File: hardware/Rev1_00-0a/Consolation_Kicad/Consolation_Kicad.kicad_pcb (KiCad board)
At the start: 6 copper layers, 137.5 x 76.6 mm, 401 parts, among them J10 61300311121, J11 5051102291, J12 RPI_CMx_B, J13 5051102291, J14 61300311121, J15 61300311121, J17 61300311121, J18 61300411121, J19 RPI_CMx_A, J2 SJ-3524-SMT-TR, J3 62684-402100ALF, J4 12401598E4#2A, J5 S2B-PH-K-S, J6 2086581001, J7 2998TR, J8 DM3AT-SF-PEJM5, Q1 SSM3K56FS,LF, Q10 SSM3K56FS,LF, Q11 SSM3K56FS,LF, Q14 SSM3K56FS,LF, Q18 SSM3K56FS,LF, Q19 SSM3K56FS,LF, Q2 SSM3K56FS,LF, Q20 SSM3K56FS,LF, Q21 SSM3K56FS,LF, Q22 SSM3K56FS,LF, Q23 SSM3K56FS,LF, Q24 SSM3K56FS,LF, Q25 SSM3K56FS,LF, Q26 SSM3K56FS,LF, Q27 SSM3K56FS,LF, Q28 SSM3K56FS,LF, Q3 SSM3K56FS,LF, Q7 SSM3K56FS,LF, Q8 SSM3K56FS,LF, Q9 SSM3K56FS,LF, U1 BQ25640VDLR, U10 TPS62826DMQR, U11 AP22913W6-7, U15 SN65DSI84ZXHR, U18 AP22913W6-7, U19 SN74LVC1G125DBVR, U2 RP2350A, U21 MCP7940NT-I/MS, U26 TPS61169DCKR, U30 STM6710DWB6F, U31 SN74LVC1G125DBVR, U32 SN74HCS365QPWRQ1, U4 ECS-2016MVQ-120-BP-TR, U5 NAU88C22YG, U6 AP22913W6-7, U7 TPS79901DRVR, U8 GD25Q32CWIGR, U9 TPS61230ARNSR, Y1 12MHz 10pF, Y2 32.768kHz

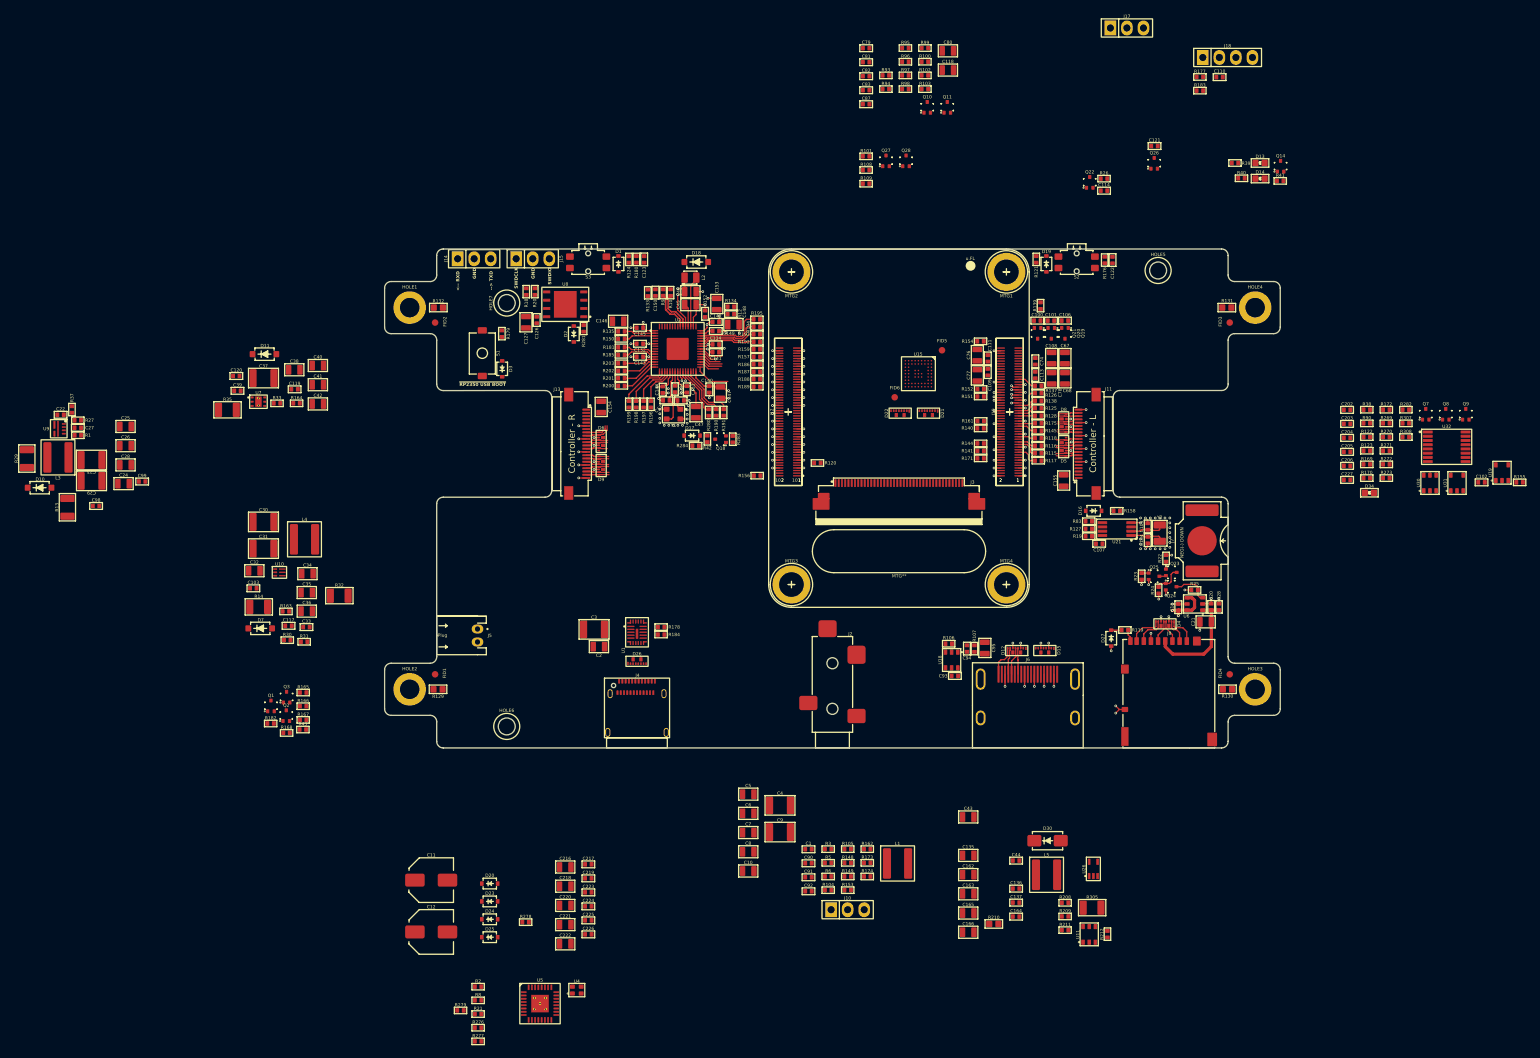
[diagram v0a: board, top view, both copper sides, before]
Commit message: Continue preliminary placement To do : Power supplies + Type C charger
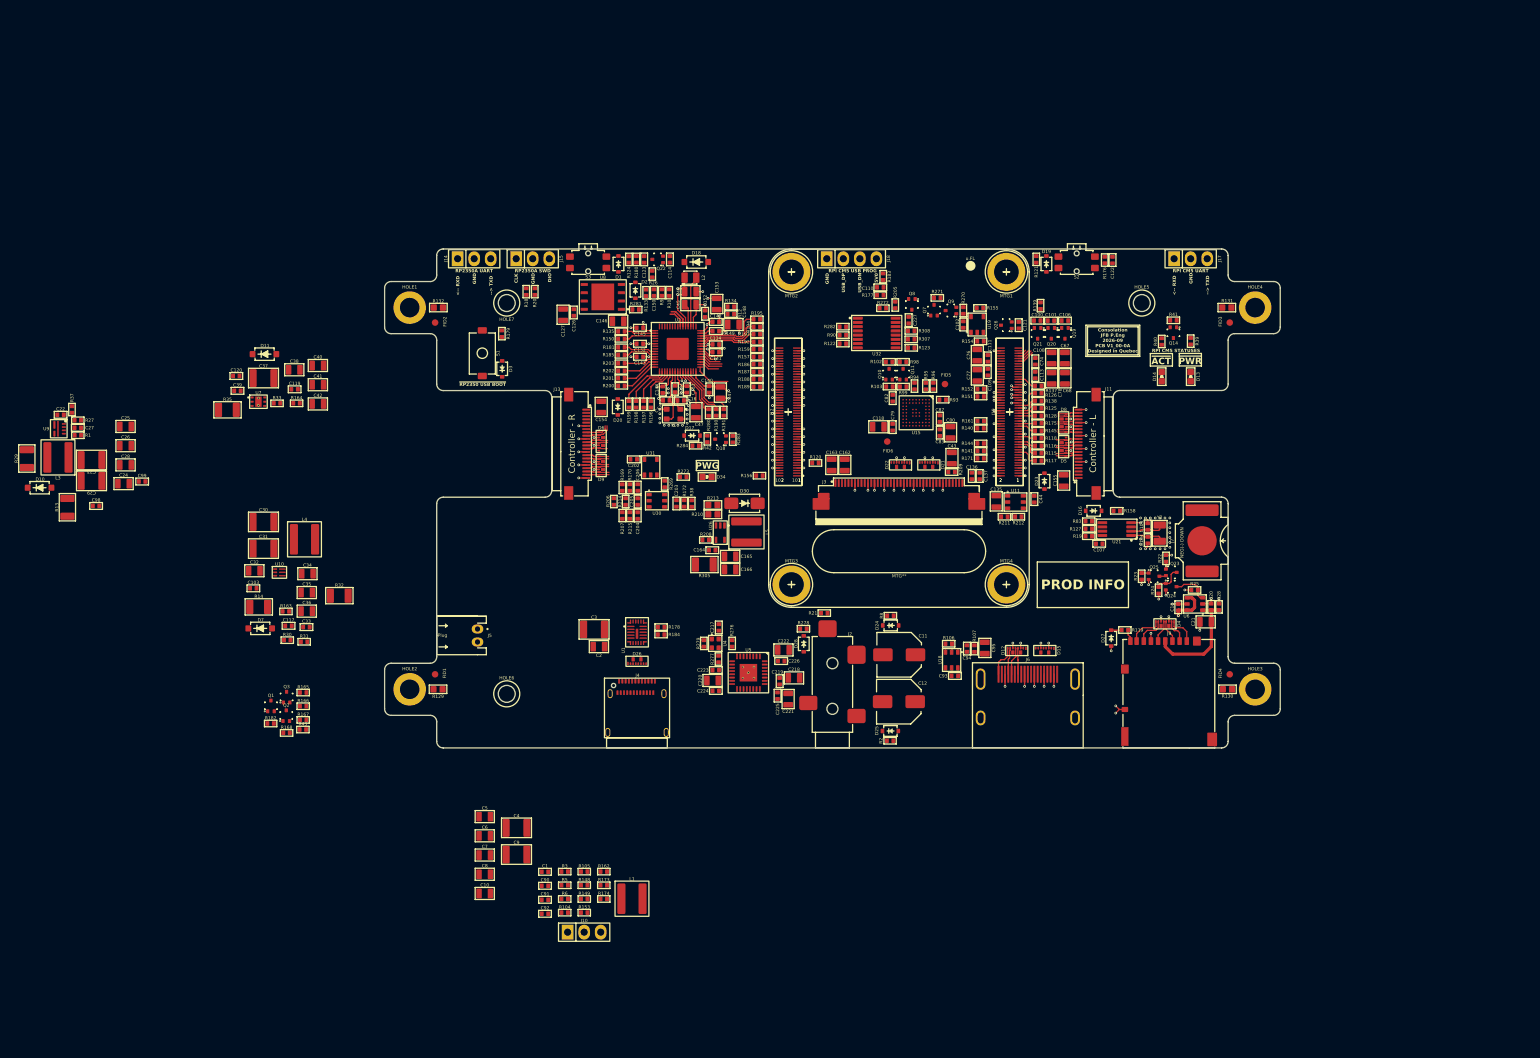
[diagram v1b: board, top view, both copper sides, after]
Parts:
- removed C216: 10u, footprint:CAP_NONPOL_0805
- removed C81: 0.1u, footprint:CAP_NONPOL_0402
- removed Q27, Q28: SSM3K56FS,LF, footprint:SC-75
- removed R100, R101, R108: 10K, footprint:RES_0402
- removed R109, R97: 0R, footprint:RES_0402
- added D28: ESD7351HT1G, footprint:SOD-323, F.Cu at (104.5, 110.7)
- added R205: 6K04, footprint:RES_0402, F.Cu at (118.5, 58.7)
- added R206: 0R, footprint:RES_0402, F.Cu at (75.3, 88.9)
- added R207: 0R, footprint:RES_0402, F.Cu at (76.6, 91.0)
- added R213: 1R5, footprint:RES_0603, F.Cu at (90.5, 89.4)
- added R214: 0R, footprint:RES_0402, F.Cu at (77.1, 88.9)
- added R215: 0R, footprint:RES_0402, F.Cu at (77.8, 91.0)
- R95, R96: value 0R -> 10K
- moved U31 123.8 mm to (81.0, 83.6)
- moved U30 118.7 mm to (81.9, 88.8), turned to -90 degrees
- moved R169 114.3 mm to (76.6, 86.7), turned to 90 degrees
- moved R170 113.1 mm to (77.8, 86.7), turned to -90 degrees
- moved R269 111.2 mm to (83.1, 86.2), turned to 90 degrees
- moved C202 109.8 mm to (78.3, 82.4)
- moved C204 109.6 mm to (79.0, 91.0), turned to 90 degrees
- moved C205 109.2 mm to (79.0, 88.9), turned to 90 degrees
- moved C206 109.0 mm to (79.0, 86.7), turned to -90 degrees
- moved R172 108.7 mm to (86.1, 89.2), turned to -90 degrees
- moved R273 107.9 mm to (86.0, 85.1)
- moved D23 106.8 mm to (141.4, 85.8), turned to -90 degrees
- moved R38 104.6 mm to (87.2, 89.2), turned to 90 degrees
- moved C203 103.7 mm to (84.9, 89.2), turned to -90 degrees
- moved D34 101.7 mm to (89.6, 85.1), turned to 180 degrees
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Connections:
- C204 pad 2: 1V8 -> Net-(U30-V3IN)
- C205 pad 2: 3V3 -> Net-(U30-V2IN)
- R272 pad 1: Net-(Q8-D) -> GND
- R272 pad 2: 3V3 -> Net-(Q8-D)
- R95 pad 1: 1V8 -> /DSI TO LVDS/SN65DSI_EN
- R95 pad 2: Net-(U15-ADDR) -> /~{DSI_BRDG_RST}
- R96 pad 1: unconnected-(R96-Pad1) -> GND
- R96 pad 2: Net-(U15-IRQ) -> /DSI TO LVDS/SN65DSI_EN
- U15 pad J9: Net-(U15-IRQ) -> unconnected-(U15-IRQ-PadJ9)
- U30 pad 2: 3V3 -> Net-(U30-V2IN)
- U30 pad 3: 1V8 -> Net-(U30-V3IN)
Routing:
- net GND: track 120.3 -> 134.4 mm, vias 139 -> 153
- net /CONTROLLER/USB_P: track 6.20 -> 2.93 mm
- net /CONTROLLER/USB_N: track 6.20 -> 3.40 mm
- net /CM5_CONN_A/~{WL_DIS}: track 0.00 -> 2.71 mm
- net /CM5_CONN_A/~{BT_DIS}: track 0.00 -> 2.45 mm
- net /CM5_CONN_A/~{RPIBOOT}: track 0.00 -> 1.98 mm
- net /CM5_CONN_A/~{RPI_LED_PWR}: track 0.00 -> 1.31 mm
- net 3V3: track 38.9 -> 38.0 mm, vias 17 -> 16
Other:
- board text added: "5V0"
- board text added: "CLK"
- board text added: "Consolation JFB P.Eng 2026-09 PCB V1_00-0A Designed in Quebec"
- board text added: "DIO"
- board text added: "PROD INFO"
- board text added: "PWG"
- board text added: "RP2350A SWD"
- board text added: "RP2350A UART"
- board text added: "RPI CM5 STATUSES"
- board text added: "RPI CM5 UART"
- board text added: "RPI CM5 USB PROG"
- board text added: "USB_DN"
- board text added: "USB_DP"
- board text added: "~{ACT}"
- board text added: "~{PWR}"
- board text removed: "SWDCLK"
- board text removed: "SWDIO"

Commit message: Preliminary placement done Add test points to PCB
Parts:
- removed C103, C117, C120, C91, C98, C99: 0.1u, footprint:CAP_NONPOL_0402
- removed C24, C32, C38: 1u, footprint:CAP_NONPOL_0805
- removed C25, C34, C41: 22u, footprint:CAP_NONPOL_0805
- removed Q2: SSM3K56FS,LF, footprint:SC-75
- removed R165, R167: 10K, footprint:RES_0402
- removed R178, R184: 0R, footprint:RES_0402
- removed R29, R32, R35: 0R, footprint:RES_1206
- added C13: 22u, footprint:CAP_NONPOL_0805, F.Cu at (83.5, 97.5)
- added D29: SMAJ20A, footprint:DO-214AC, F.Cu at (84.8, 114.3)
- added R108: 4K7, footprint:RES_0402, F.Cu at (127.0, 65.0)
- added R7: 103AT-4-70374, footprint:HEADER_2P_2_54MM, F.Cu at (56.9, 125.2)
- added TP1: 75 mils, footprint:SMT_TP_75_MILS, B.Cu at (167.4, 66.2)
- added TP10: 75 mils, footprint:SMT_TP_75_MILS, B.Cu at (70.2, 101.6)
- added TP11: 75 mils, footprint:SMT_TP_75_MILS, B.Cu at (61.5, 90.0)
- added TP12: 75 mils, footprint:SMT_TP_75_MILS, B.Cu at (50.0, 97.8)
- added TP13: 75 mils, footprint:SMT_TP_75_MILS, B.Cu at (61.5, 94.4)
- added TP14: 75 mils, footprint:SMT_TP_75_MILS, B.Cu at (59.1, 91.5)
- added TP15: 75 mils, footprint:SMT_TP_75_MILS, B.Cu at (81.0, 79.8)
- added TP16: 75 mils, footprint:SMT_TP_75_MILS, B.Cu at (110.1, 59.3)
- added TP17: 75 mils, footprint:SMT_TP_75_MILS, B.Cu at (131.0, 56.8)
- added TP18: 75 mils, footprint:SMT_TP_75_MILS, B.Cu at (156.4, 98.0)
- added TP19: 75 mils, footprint:SMT_TP_75_MILS, B.Cu at (167.8, 107.5)
- added TP2: 75 mils, footprint:SMT_TP_75_MILS, B.Cu at (142.8, 90.8)
- added TP20: 75 mils, footprint:SMT_TP_75_MILS, B.Cu at (101.9, 108.4)
- added TP21: 75 mils, footprint:SMT_TP_75_MILS, B.Cu at (94.5, 121.0)
- added TP22: 75 mils, footprint:SMT_TP_75_MILS, B.Cu at (91.4, 121.0)
- added TP23: 75 mils, footprint:SMT_TP_75_MILS, B.Cu at (106.8, 80.3)
- added TP24: 75 mils, footprint:SMT_TP_75_MILS, B.Cu at (141.3, 56.2)
- added TP25: 75 mils, footprint:SMT_TP_75_MILS, B.Cu at (92.5, 52.8)
- added TP26: 75 mils, footprint:SMT_TP_75_MILS, B.Cu at (98.3, 110.1)
- added TP27: 75 mils, footprint:SMT_TP_75_MILS, B.Cu at (94.0, 105.8)
- added TP28: 75 mils, footprint:SMT_TP_75_MILS, B.Cu at (94.0, 102.2)
- added TP29: 75 mils, footprint:SMT_TP_75_MILS, B.Cu at (97.4, 102.0)
- added TP3: 75 mils, footprint:SMT_TP_75_MILS, B.Cu at (65.0, 114.2)
- added TP30: 75 mils, footprint:SMT_TP_75_MILS, B.Cu at (112.5, 116.0)
- added TP31: 75 mils, footprint:SMT_TP_75_MILS, B.Cu at (105.2, 123.0)
- added TP32: 75 mils, footprint:SMT_TP_75_MILS, B.Cu at (149.1, 83.8)
- added TP33: 75 mils, footprint:SMT_TP_75_MILS, B.Cu at (68.3, 76.8)
- added TP34: 75 mils, footprint:SMT_TP_75_MILS, B.Cu at (85.4, 82.5)
- added TP35: 75 mils, footprint:SMT_TP_75_MILS, B.Cu at (73.8, 61.0)
- added TP36: 75 mils, footprint:SMT_TP_75_MILS, B.Cu at (88.0, 52.4)
- added TP37: 75 mils, footprint:SMT_TP_75_MILS, B.Cu at (89.7, 112.0)
- added TP38: 75 mils, footprint:SMT_TP_75_MILS, B.Cu at (60.1, 112.7)
- added TP39: 75 mils, footprint:SMT_TP_75_MILS, B.Cu at (75.5, 114.4)
- added TP4: 75 mils, footprint:SMT_TP_75_MILS, B.Cu at (147.7, 110.5)
- added TP40: 75 mils, footprint:SMT_TP_75_MILS, B.Cu at (82.0, 114.3)
- added TP41: 75 mils, footprint:SMT_TP_75_MILS, B.Cu at (74.5, 102.3)
- added TP42: 75 mils, footprint:SMT_TP_75_MILS, B.Cu at (84.8, 101.0)
- added TP43: 75 mils, footprint:SMT_TP_75_MILS, B.Cu at (72.4, 114.7)
- added TP44: 75 mils, footprint:SMT_TP_75_MILS, B.Cu at (79.7, 101.7)
- added TP45: 75 mils, footprint:SMT_TP_75_MILS, B.Cu at (131.0, 88.4)
- added TP46: 75 mils, footprint:SMT_TP_75_MILS, B.Cu at (101.2, 89.2)
- added TP47: 75 mils, footprint:SMT_TP_75_MILS, B.Cu at (89.8, 86.3)
- added TP48: 75 mils, footprint:SMT_TP_75_MILS, B.Cu at (134.3, 115.6)
- added TP49: 75 mils, footprint:SMT_TP_75_MILS, B.Cu at (61.4, 122.7)
- added TP5: 75 mils, footprint:SMT_TP_75_MILS, B.Cu at (83.3, 93.3)
- added TP50: 75 mils, footprint:SMT_TP_75_MILS, B.Cu at (124.9, 62.9)
- added TP51: 75 mils, footprint:SMT_TP_75_MILS, B.Cu at (125.2, 68.7)
- added TP6: 75 mils, footprint:SMT_TP_75_MILS, B.Cu at (97.5, 106.5)
- added TP7: 75 mils, footprint:SMT_TP_75_MILS, B.Cu at (69.3, 68.2)
- added TP8: 75 mils, footprint:SMT_TP_75_MILS, B.Cu at (50.5, 90.8)
- added TP9: 75 mils, footprint:SMT_TP_75_MILS, B.Cu at (76.7, 99.6)
- moved Q1 117.9 mm to (127.8, 67.0), turned to 90 degrees
- moved R166 113.3 mm to (128.7, 69.2), turned to 90 degrees
- moved R37 87.1 mm to (76.8, 94.9), turned to 180 degrees
- moved R13 86.6 mm to (77.7, 97.0), turned to 180 degrees
- moved L3 83.9 mm to (72.5, 97.0), turned to 90 degrees
- moved C22 81.7 mm to (70.7, 90.7)
- moved U9 81.7 mm to (70.2, 92.8)
- moved R1 81.5 mm to (73.2, 93.0)
- moved C27 81.5 mm to (73.2, 91.8)
- moved R27 81.5 mm to (73.2, 90.7)
- moved D10 76.9 mm to (63.9, 91.9), turned to -90 degrees
- moved C29 73.7 mm to (68.0, 97.0), turned to -90 degrees
- moved C23 71.2 mm to (64.8, 97.0), turned to -90 degrees
- moved C28 68.3 mm to (67.9, 92.7), turned to 90 degrees
- moved C26 66.8 mm to (66.0, 92.8), turned to 90 degrees
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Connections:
- C26 pad 2: Net-(D10-K) -> 5V0
- C27 pad 2: Net-(D10-K) -> 5V0
- C28 pad 2: Net-(D10-K) -> 5V0
- C33 pad 2: Net-(D7-K) -> 3V3
- C35 pad 2: Net-(D7-K) -> 3V3
- C36 pad 2: Net-(D7-K) -> 3V3
- C39 pad 2: Net-(D11-K) -> 1V8
- C40 pad 2: Net-(D11-K) -> 1V8
- C42 pad 2: Net-(D11-K) -> 1V8
- D10 pad 1: Net-(D10-K) -> 5V0
- D11 pad 1: Net-(D11-K) -> 1V8
- D7 pad 1: Net-(D7-K) -> 3V3
- L4 pad 2: Net-(D7-K) -> 3V3
- Q1 pad 1: 1V8_CMx -> 3V3_CMx
- Q1 pad 2: Net-(Q1-S) -> GND
- R163 pad 2: Net-(D7-K) -> 3V3
- R166 pad 2: 1V8_CMx -> 3V3_CMx
- R27 pad 2: Net-(D10-K) -> 5V0
- R30 pad 2: Net-(D7-K) -> 3V3
- R33 pad 2: Net-(D11-K) -> 1V8
- U1 pad 20: Net-(U1-D-) -> unconnected-(U1-D--Pad20)
- U1 pad 21: Net-(U1-D+) -> unconnected-(U1-D+-Pad21)
- U7 pad 1: Net-(D11-K) -> 1V8
- U9 pad 7: Net-(D10-K) -> 5V0
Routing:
- net /CM5_CONN_A/SDIO_D1: track 6.37 -> 3.48 mm
- net /CM5_CONN_A/SDIO_D0: track 5.80 -> 3.50 mm
- net /CM5_CONN_A/SDIO_D2: track 5.58 -> 3.29 mm
- net /CM5_CONN_A/SDIO_D3: track 4.88 -> 2.77 mm
- net /CM5_CONN_A/SDIO_CMD: track 4.59 -> 2.83 mm
- net /CM5_CONN_A/SDIO_CLK: track 4.45 -> 2.80 mm
- net GND: track 134.4 -> 133.1 mm, vias 153 -> 152
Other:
- board text added: "-> TXD"
- board text added: "<- RXD"
- board text added: "BAT CHRG"
- board text added: "BAT NTC THERM"
- board text added: "CTRL - L"
- board text added: "CTRL - R"
- board text added: "Consolation JFB P.Eng 2026-10 PCB V1_00-0A Designed in Quebec"
- board text added: "DIS"
- board text added: "SER INFO"
- board text added: "Solder on bottom"
- board text added: "~{EN}"
- board text removed: "--> TXD"
- board text removed: "<-- RXD"
- board text removed: "Consolation JFB P.Eng 2026-09 PCB V1_00-0A Designed in Quebec"
- board text removed: "Controller - L"
- board text removed: "Controller - R"
